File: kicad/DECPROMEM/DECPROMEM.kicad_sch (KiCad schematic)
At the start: 136 parts, among them J10 BDAL08, J100 A15, J101 A16, J102 A17, J103 A18, J104 A19, J105 A20, J106 A21, J11 BDAL09, J12 BDAL10, J13 BDAL11, J14 BDAL12, J15 BDAL13, J16 BDAL14, J17 BDAL15, J18 BDAL16, J19 BDAL17, J2 BDAL00, J20 BDAL18, J21 BDAL19, J22 BDAL20, J23 BDAL21, J24 BRPLYL, J25 BMDENL, J26 BWRITEL, J27 BWLBL, J28 BWHBL, J29 BSDENL, J3 BDAL01, J30 SSnL, J31 BDSL, J32 BASL, J33 BIOSELL, J34 BDCOKH, J35 GND, J36 GND, J37 GND, J38 DAH00, J39 DAH01, J4 BDAL02, J40 DAH02, J41 DAH03, J42 DAH04, J43 DAH05, J44 DAH06, J45 DAH07, J46 DAH08, J47 DAH09, J48 DAH10, J49 DAH11, J5 BDAL03, J50 DAH12, J51 DAH13, J52 DAH14, J53 DAH15, J54 DAH16, J55 DAH17, J56 DAH18, J57 DAH19, J58 DAH20, J59 DAH21, J6 BDAL04, J60 JTAG, J61 ASL, J62 MDENL, J63 SDENL, J64 MOEL, J65 MWEL, J66 MCEHIGHL, J67 MCELOWH, J68 MLEL, J69 MHEL, J7 BDAL05, J70 BUSDIR, J71 BUSOE, J72 CLK, J73 MA15, J74 MA16, J75 MA17, J76 MA18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

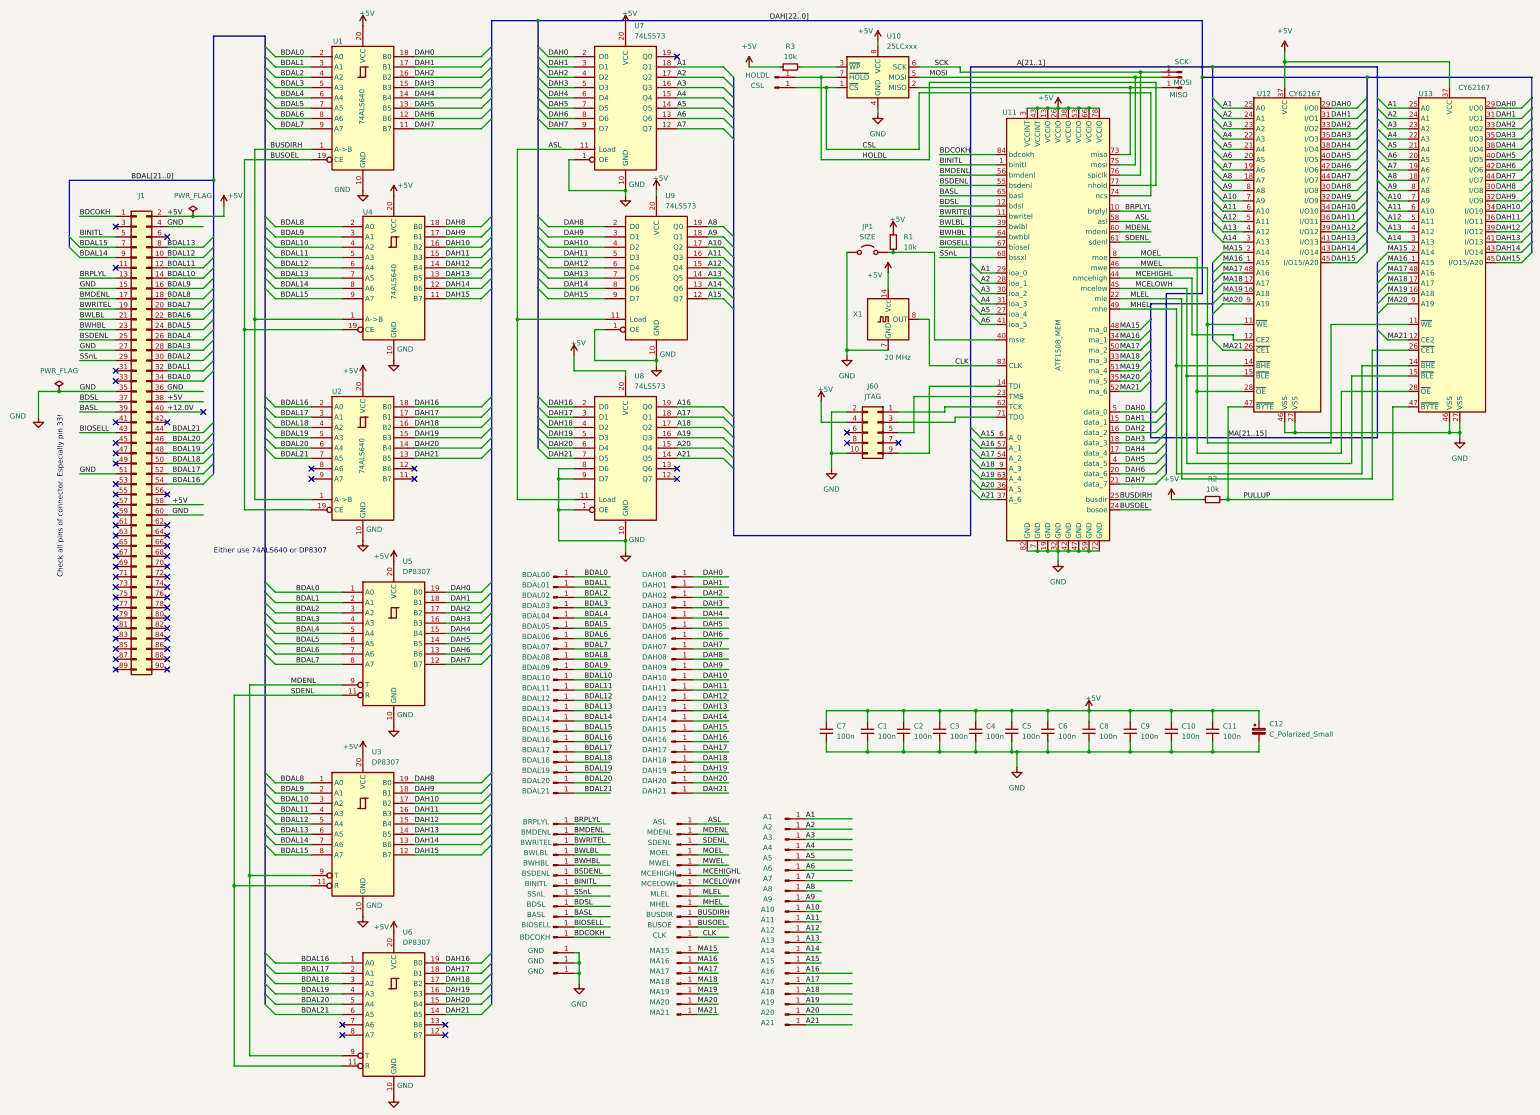
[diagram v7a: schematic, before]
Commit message: Updated the schematics and layout to fix a bunch small errors.
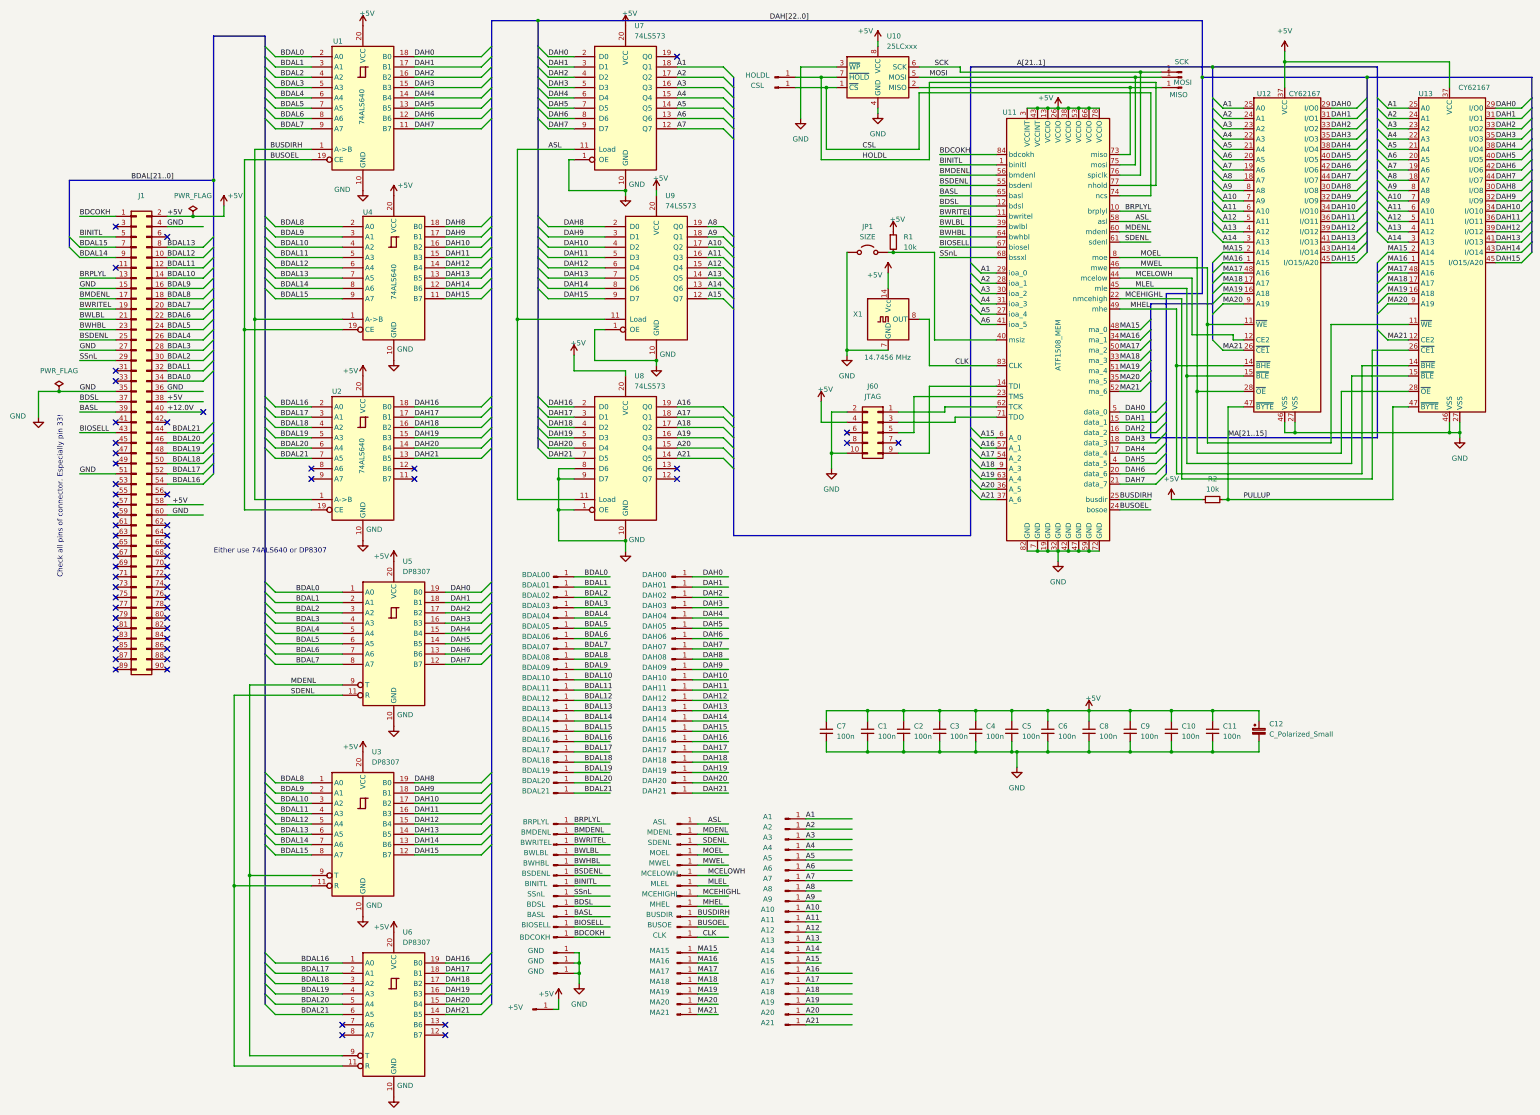
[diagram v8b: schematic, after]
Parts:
- removed R3: 10k, Resistor_THT:R_Axial_DIN0207_L6.3mm_D2.5mm_P10.16mm_Horizontal, symbol Device:R_Small
- added J107: +5V, CompLibFootprint:Testpoint, symbol Connector:Conn_01x01_Pin
- J66: value MCEHIGHL -> MCELOWH
- J67: value MCELOWH -> MLEL
- J68: value MLEL -> MCEHIGHL
- X1: value 20 MHz -> 14.7456 MHz
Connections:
- net +5V: now also J107.1 (Pin_1)
- net GND: now also U10.3 (~{WP})
- net MCEHIGHL: now also J68.1 (Pin_1), U11.22 (nmcehigh), U13.26 (~{CE1}); no longer J66.1 (Pin_1), U11.44 (nmcehigh), U12.12 (CE2)
- net MCELOWH: now also J66.1 (Pin_1), U11.44 (mcelow), U12.12 (CE2); no longer J67.1 (Pin_1), U11.45 (mcelow), U12.15 (~{BLE}), U13.15 (~{BLE})
- net MLEL: now also J67.1 (Pin_1), U11.45 (mle), U12.15 (~{BLE}), U13.15 (~{BLE}); no longer J68.1 (Pin_1), U11.22 (mle), U13.26 (~{CE1})
